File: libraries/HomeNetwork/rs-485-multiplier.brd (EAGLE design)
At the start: 70.8 x 34.3 mm, 4 parts, among them X1 RJ45-6L21-S, X2 RJ45-6L21-S, X3 RJ45-6L21-S, X4 RJ45-6L21-S

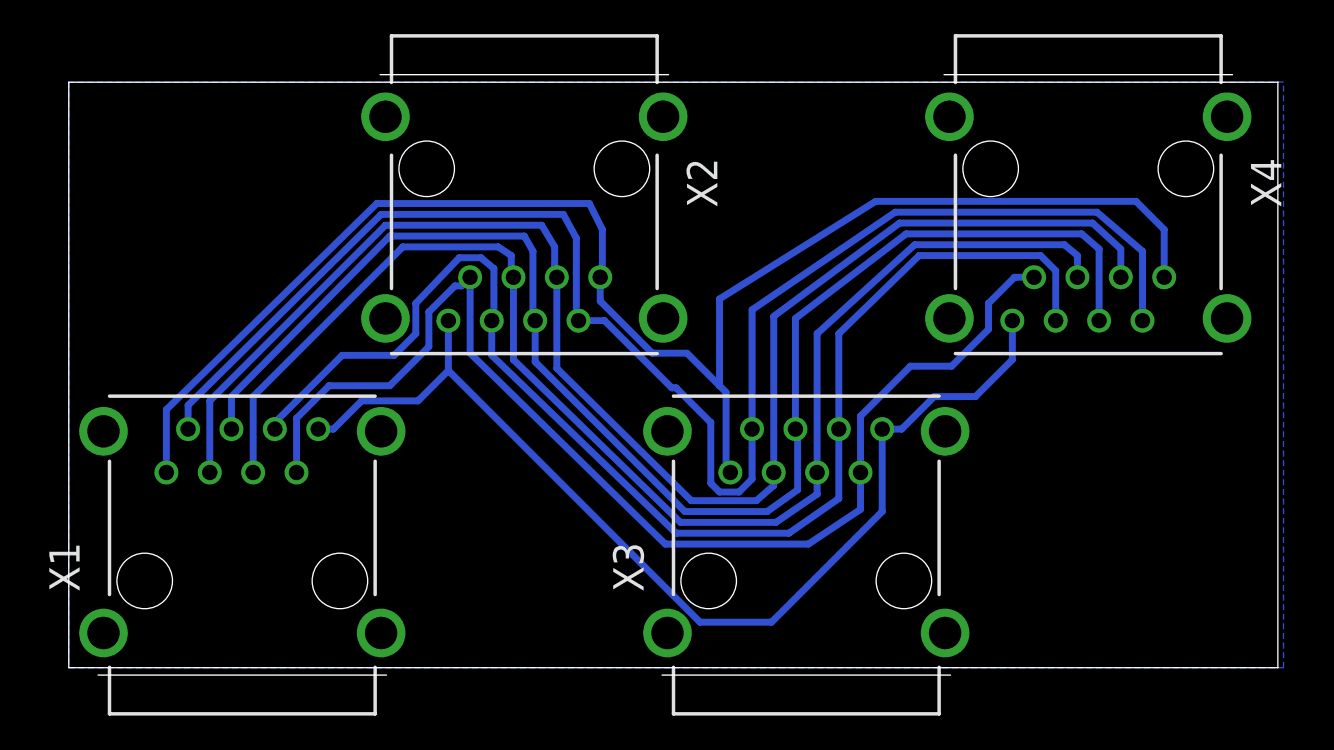
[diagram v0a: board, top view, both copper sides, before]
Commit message: Adjusted RS-485 splitter to ignore mounting holes to make room for routes
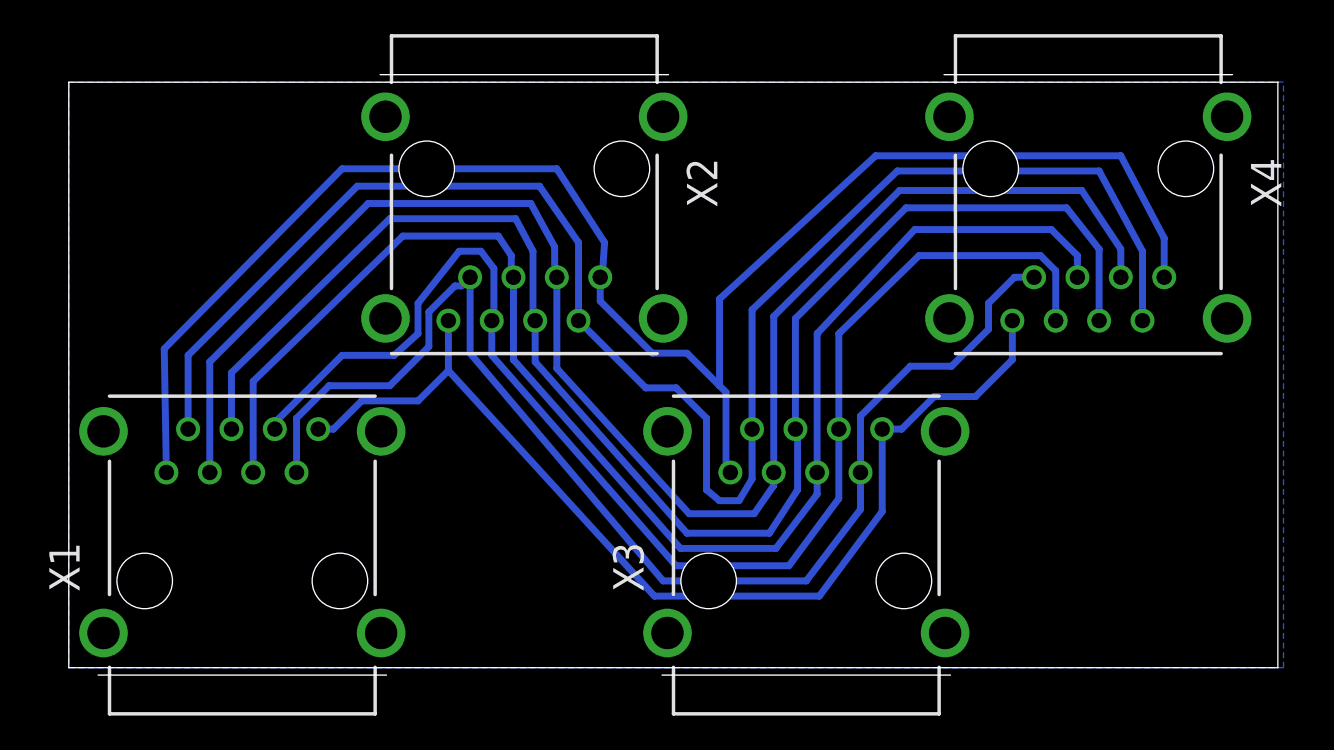
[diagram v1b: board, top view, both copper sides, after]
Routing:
- net N$2: track 90.6 -> 98.1 mm
- net N$1: track 89.9 -> 97.2 mm
- net N$3: track 87.0 -> 93.3 mm
- net N$4: track 84.0 -> 89.5 mm
- net N$5: track 79.8 -> 84.2 mm
- net N$6: track 76.3 -> 79.6 mm
- net N$7: track 70.3 -> 73.4 mm
